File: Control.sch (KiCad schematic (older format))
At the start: 1 part

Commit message: no message
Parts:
- removed U?: WeMos_mini, symbol bambouLab:WeMos_mini
- added U?: WeMos_mini, symbol bambouLab:WeMos_mini
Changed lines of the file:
@@
 $Descr A4 11693 8268
 encoding utf-8
-Sheet 2 3
+Sheet 5 5
 Title ""
 Date ""
@@
 $Comp
 L bambouLab:WeMos_mini U?
-U 1 1 5D8F17D5
-P 5500 3650
-F 0 "U?" H 5500 4393 60  0000 C CNN
-F 1 "WeMos_mini" H 5500 4287 60  0000 C CNN
-F 2 "" H 6050 2950 60  0000 C CNN
-F 3 "http://www.wemos.cc/Products/d1_mini.html" H 5500 4181 60  0000 C CNN
-	1    5500 3650
+U 1 1 5D974EC7
+P 5700 4000
+F 0 "U?" H 5700 4637 60  0000 C CNN
+F 1 "WeMos_mini" H 5700 4531 60  0000 C CNN
+F 2 "" H 6250 3300 60  0000 C CNN
+F 3 "" H 5700 4531 60  0000 C CNN
+	1    5700 4000
 	1    0    0    -1
 $EndComp

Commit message: no message
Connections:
- net labels added: 3V3, 5V, BLANK, DP1, DP2, DP3, DP4, DP5, DP6, GND, SHIFTCLK, STORAGECLK, TUBETX
- wire segments 0 -> 13
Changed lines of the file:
@@
 $Descr A4 11693 8268
 encoding utf-8
-Sheet 5 5
+Sheet 3 5
 Title ""
 Date ""
@@
 	1    0    0    -1
 $EndComp
+Text HLabel 4500 3950 0    50   Input ~ 0
+BLANK
+Text HLabel 4500 3850 0    50   Input ~ 0
+TUBETX
+Text HLabel 4500 4050 0    50   Input ~ 0
+SHIFTCLK
+Text HLabel 4500 4150 0    50   Input ~ 0
+STORAGECLK
+Wire Wire Line
+	5200 4150 4500 4150
+Wire Wire Line
+	4500 4050 5200 4050
+Wire Wire Line
+	5200 3950 4500 3950
+Wire Wire Line
+	4500 3850 5200 3850
+Text HLabel 5000 3650 0    50   Input ~ 0
+5V
+Wire Wire Line
+	5000 3650 5200 3650
+$Comp
+L power:GND #PWR?
+U 1 1 5DBC6996
+P 5100 3750
+F 0 "#PWR?" H 5100 3500 50  0001 C CNN
+F 1 "GND" V 5105 3622 50  0000 R CNN
+F 2 "" H 5100 3750 50  0001 C CNN
+F 3 "" H 5100 3750 50  0001 C CNN
+	1    5100 3750
+	0    1    1    0
+$EndComp
+Wire Wire Line
+	5100 3750 5200 3750
+Text HLabel 6350 4250 2    50   Input ~ 0
+DP6
+Text HLabel 6350 4150 2    50   Input ~ 0
+DP5
+Text HLabel 6350 4050 2    50   Input ~ 0
+DP4
+Text HLabel 6350 3950 2    50   Input ~ 0
+DP3
+Text HLabel 6350 3850 2    50   Input ~ 0
+DP2
+Text HLabel 6350 3750 2    50   Input ~ 0
+DP1
+Wire Wire Line
+	6200 3750 6350 3750
+Wire Wire Line
+	6200 3850 6350 3850
+Wire Wire Line
+	6350 3950 6200 3950
+Wire Wire Line
+	6200 4050 6350 4050
+Wire Wire Line
+	6350 4150 6200 4150
+Wire Wire Line
+	6200 4250 6350 4250
+Text HLabel 6350 3650 2    50   Input ~ 0
+3V3
+Wire Wire Line
+	6200 3650 6350 3650
 $EndSCHEMATC

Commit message: Finished draft schema
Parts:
- gave numbers to parts that had none: 1
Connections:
- net labels removed: 3V3, DP1, DP2, DP3, DP4, DP5, DP6
- wire segments 13 -> 6
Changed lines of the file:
@@
 $Descr A4 11693 8268
 encoding utf-8
-Sheet 3 5
+Sheet 2 5
 Title ""
 Date ""
@@
 $EndDescr
 $Comp
-L bambouLab:WeMos_mini U?
+L bambouLab:WeMos_mini U1
 U 1 1 5D974EC7
 P 5700 4000
-F 0 "U?" H 5700 4637 60  0000 C CNN
+F 0 "U1" H 5700 4637 60  0000 C CNN
 F 1 "WeMos_mini" H 5700 4531 60  0000 C CNN
 F 2 "" H 6250 3300 60  0000 C CNN
@@
 	5000 3650 5200 3650
 $Comp
-L power:GND #PWR?
+L power:GND #PWR01
 U 1 1 5DBC6996
 P 5100 3750
-F 0 "#PWR?" H 5100 3500 50  0001 C CNN
+F 0 "#PWR01" H 5100 3500 50  0001 C CNN
 F 1 "GND" V 5105 3622 50  0000 R CNN
 F 2 "" H 5100 3750 50  0001 C CNN
@@
 Wire Wire Line
 	5100 3750 5200 3750
-Text HLabel 6350 4250 2    50   Input ~ 0
-DP6
-Text HLabel 6350 4150 2    50   Input ~ 0
-DP5
-Text HLabel 6350 4050 2    50   Input ~ 0
-DP4
-Text HLabel 6350 3950 2    50   Input ~ 0
-DP3
-Text HLabel 6350 3850 2    50   Input ~ 0
-DP2
-Text HLabel 6350 3750 2    50   Input ~ 0
-DP1
-Wire Wire Line
-	6200 3750 6350 3750
-Wire Wire Line
-	6200 3850 6350 3850
-Wire Wire Line
-	6350 3950 6200 3950
-Wire Wire Line
-	6200 4050 6350 4050
-Wire Wire Line
-	6350 4150 6200 4150
-Wire Wire Line
-	6200 4250 6350 4250
-Text HLabel 6350 3650 2    50   Input ~ 0
-3V3
-Wire Wire Line
-	6200 3650 6350 3650
 $EndSCHEMATC

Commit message: Finished schema and started PCB layout
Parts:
- added J1: Conn_01x08_Female, Connector_PinHeader_2.54mm:PinHeader_1x08_P2.54mm_Vertical, symbol Connector:Conn_01x08_Female
- added J2: Conn_01x02_Female, Connector_PinHeader_2.54mm:PinHeader_1x02_P2.54mm_Vertical, symbol Connector:Conn_01x02_Female
- U1: footprint (none) -> BamboulabFootprints:D1_mini_board
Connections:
- wire segments 6 -> 16
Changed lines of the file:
@@
 F 0 "U1" H 5700 4637 60  0000 C CNN
 F 1 "WeMos_mini" H 5700 4531 60  0000 C CNN
-F 2 "" H 6250 3300 60  0000 C CNN
+F 2 "BamboulabFootprints:D1_mini_board" H 6250 3300 60  0001 C CNN
 F 3 "" H 5700 4531 60  0000 C CNN
 	1    5700 4000
@@
 Wire Wire Line
 	5100 3750 5200 3750
+$Comp
+L Connector:Conn_01x08_Female J1
+U 1 1 5D97A7C7
+P 6600 3950
+F 0 "J1" H 6628 3926 50  0000 L CNN
+F 1 "Conn_01x08_Female" H 6628 3835 50  0000 L CNN
+F 2 "Connector_PinHeader_2.54mm:PinHeader_1x08_P2.54mm_Vertical" H 6600 3950 50  0001 C CNN
+F 3 "~" H 6600 3950 50  0001 C CNN
+	1    6600 3950
+	1    0    0    -1
+$EndComp
+Wire Wire Line
+	6400 3650 6200 3650
+Wire Wire Line
+	6200 3750 6400 3750
+Wire Wire Line
+	6400 3850 6200 3850
+Wire Wire Line
+	6200 3950 6400 3950
+Wire Wire Line
+	6400 4050 6200 4050
+Wire Wire Line
+	6200 4150 6400 4150
+Wire Wire Line
+	6400 4250 6200 4250
+Wire Wire Line
+	6200 4350 6400 4350
+$Comp
+L Connector:Conn_01x02_Female J2
+U 1 1 5D97C070
+P 4800 4350
+F 0 "J2" H 4900 4350 50  0000 C CNN
+F 1 "Conn_01x02_Female" H 4850 4450 50  0000 C CNN
+F 2 "Connector_PinHeader_2.54mm:PinHeader_1x02_P2.54mm_Vertical" H 4800 4350 50  0001 C CNN
+F 3 "~" H 4800 4350 50  0001 C CNN
+	1    4800 4350
+	-1   0    0    1
+$EndComp
+Wire Wire Line
+	5200 4250 5000 4250
+Wire Wire Line
+	5000 4350 5200 4350
 $EndSCHEMATC

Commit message: 90% routed
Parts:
- U1: symbol bambouLab:WeMos_mini -> nixieClock_ZM1000-rescue:WeMos_mini-bambouLab
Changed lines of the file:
@@
 $EndDescr
 $Comp
-L bambouLab:WeMos_mini U1
+L nixieClock_ZM1000-rescue:WeMos_mini-bambouLab U1
 U 1 1 5D974EC7
 P 5700 4000
+AR Path="/5D974EC7" Ref="U1"  Part="1"
+AR Path="/5D9058C6/5D974EC7" Ref="U1"  Part="1"
 F 0 "U1" H 5700 4637 60  0000 C CNN
 F 1 "WeMos_mini" H 5700 4531 60  0000 C CNN

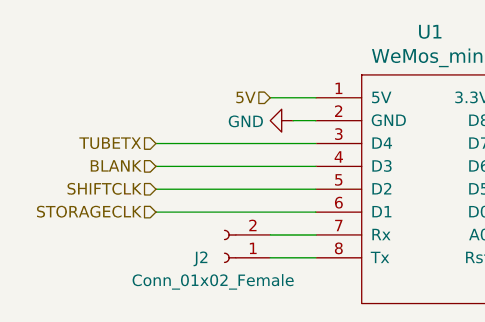
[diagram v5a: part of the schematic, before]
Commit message: Completed layout inc optimisation of data pattern for shift registers
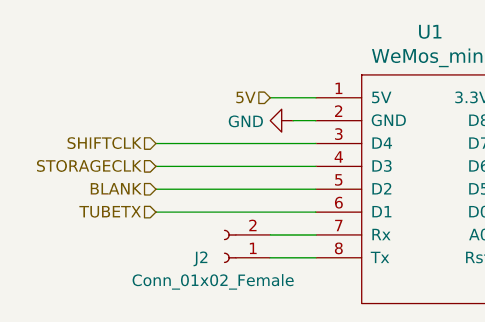
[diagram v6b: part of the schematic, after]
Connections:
- net BLANK: now also U1.5 (D2); no longer U1.4 (D3)
- net SHIFTCLK: now also U1.3 (D4); no longer U1.5 (D2)
- net STORAGECLK: now also U1.4 (D3); no longer U1.6 (D1)
- net TUBETX: now also U1.6 (D1); no longer U1.3 (D4)
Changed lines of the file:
@@
 	1    0    0    -1
 $EndComp
+Text HLabel 4500 4050 0    50   Input ~ 0
+BLANK
+Text HLabel 4500 4150 0    50   Input ~ 0
+TUBETX
+Text HLabel 4500 3850 0    50   Input ~ 0
+SHIFTCLK
 Text HLabel 4500 3950 0    50   Input ~ 0
-BLANK
-Text HLabel 4500 3850 0    50   Input ~ 0
-TUBETX
-Text HLabel 4500 4050 0    50   Input ~ 0
-SHIFTCLK
-Text HLabel 4500 4150 0    50   Input ~ 0
 STORAGECLK
 Wire Wire Line

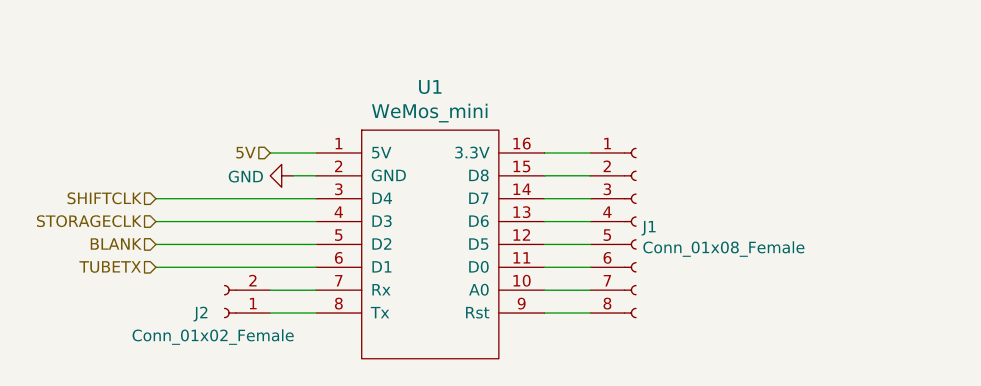
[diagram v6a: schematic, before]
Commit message: Szitched to DIP shift registers, added BME280
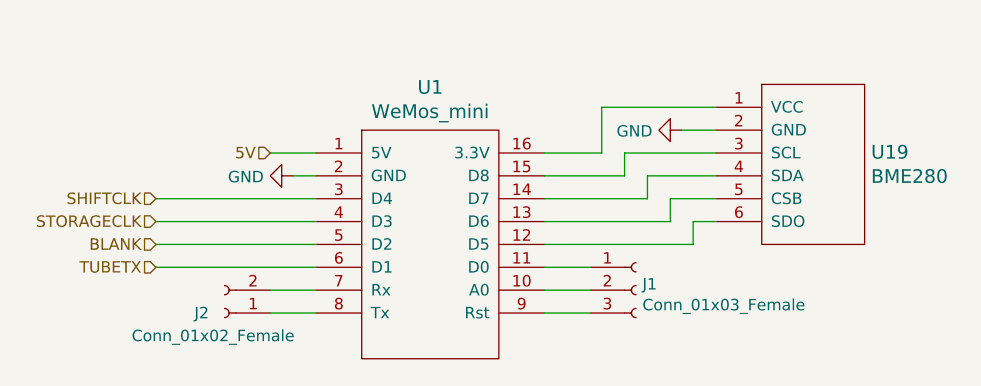
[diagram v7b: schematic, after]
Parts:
- removed J1: Conn_01x08_Female, Connector_PinHeader_2.54mm:PinHeader_1x08_P2.54mm_Vertical, symbol Connector:Conn_01x08_Female
- added J1: Conn_01x03_Female, Connector_PinHeader_2.54mm:PinHeader_1x03_P2.54mm_Vertical, symbol Connector:Conn_01x03_Female
- added U19: BME280, nixies:BME280, symbol bambouLab:BME280
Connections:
- net GND: now also U19.2 (GND)
- net at U1.10 (A0): now also J1.2 (Pin_2)
- net at U1.11 (D0): now also J1.1 (Pin_1)
- net at U1.12 (D5): now also U19.6 (SDO)
- net at U1.13 (D6): now also U19.5 (CSB)
- net at U1.14 (D7): now also U19.4 (SDA)
- net at U1.15 (D8): now also U19.3 (SCL)
- net at U1.16 (3.3V): now also U19.1 (VCC)
- net at U1.9 (Rst): now also J1.3 (Pin_3)
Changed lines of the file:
@@
 Wire Wire Line
 	5100 3750 5200 3750
-$Comp
-L Connector:Conn_01x08_Female J1
-U 1 1 5D97A7C7
-P 6600 3950
-F 0 "J1" H 6628 3926 50  0000 L CNN
-F 1 "Conn_01x08_Female" H 6628 3835 50  0000 L CNN
-F 2 "Connector_PinHeader_2.54mm:PinHeader_1x08_P2.54mm_Vertical" H 6600 3950 50  0001 C CNN
-F 3 "~" H 6600 3950 50  0001 C CNN
-	1    6600 3950
-	1    0    0    -1
-$EndComp
-Wire Wire Line
-	6400 3650 6200 3650
-Wire Wire Line
-	6200 3750 6400 3750
-Wire Wire Line
-	6400 3850 6200 3850
-Wire Wire Line
-	6200 3950 6400 3950
-Wire Wire Line
-	6400 4050 6200 4050
-Wire Wire Line
-	6200 4150 6400 4150
 Wire Wire Line
 	6400 4250 6200 4250
@@
 Wire Wire Line
 	5000 4350 5200 4350
+Wire Wire Line
+	6200 4150 6400 4150
+$Comp
+L bambouLab:BME280 U19
+U 1 1 5DA4BB9B
+P 7400 3800
+F 0 "U19" H 7628 3953 60  0000 L CNN
+F 1 "BME280" H 7628 3847 60  0000 L CNN
+F 2 "nixies:BME280" H 7400 3800 60  0001 C CNN
+F 3 "" H 7400 3800 60  0001 C CNN
+	1    7400 3800
+	1    0    0    -1
+$EndComp
+Wire Wire Line
+	6950 3850 6750 3850
+Wire Wire Line
+	6750 3850 6750 3950
+Wire Wire Line
+	6200 3950 6750 3950
+Wire Wire Line
+	6650 3850 6650 3750
+Wire Wire Line
+	6650 3750 6950 3750
+Wire Wire Line
+	6200 3850 6650 3850
+Wire Wire Line
+	6550 3750 6550 3650
+Wire Wire Line
+	6550 3650 6950 3650
+Wire Wire Line
+	6200 3750 6550 3750
+Wire Wire Line
+	6950 3950 6850 3950
+Wire Wire Line
+	6850 3950 6850 4050
+Wire Wire Line
+	6200 4050 6850 4050
+Wire Wire Line
+	6450 3650 6450 3450
+Wire Wire Line
+	6450 3450 6950 3450
+Wire Wire Line
+	6200 3650 6450 3650
+Wire Wire Line
+	6950 3550 6800 3550
+$Comp
+L power:GND #PWR0106
+U 1 1 5DA50DD3
+P 6800 3550
+F 0 "#PWR0106" H 6800 3300 50  0001 C CNN
+F 1 "GND" V 6805 3422 50  0000 R CNN
+F 2 "" H 6800 3550 50  0001 C CNN
+F 3 "" H 6800 3550 50  0001 C CNN
+	1    6800 3550
+	0    1    1    0
+$EndComp
+$Comp
+L Connector:Conn_01x03_Female J1
+U 1 1 5DA53641
+P 6600 4250
+F 0 "J1" H 6628 4276 50  0000 L CNN
+F 1 "Conn_01x03_Female" H 6628 4185 50  0000 L CNN
+F 2 "Connector_PinHeader_2.54mm:PinHeader_1x03_P2.54mm_Vertical" H 6600 4250 50  0001 C CNN
+F 3 "~" H 6600 4250 50  0001 C CNN
+	1    6600 4250
+	1    0    0    -1
+$EndComp
 $EndSCHEMATC

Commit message: Final pending check
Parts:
- U19: symbol bambouLab:BME280 -> nixieClock_ZM1000-rescue:BME280-bambouLab
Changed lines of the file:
@@
 	6200 4150 6400 4150
 $Comp
-L bambouLab:BME280 U19
+L nixieClock_ZM1000-rescue:BME280-bambouLab U19
 U 1 1 5DA4BB9B
 P 7400 3800
